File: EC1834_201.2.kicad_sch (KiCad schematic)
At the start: 69 parts, among them X4 Lautsprecher, X7 DB9_Female

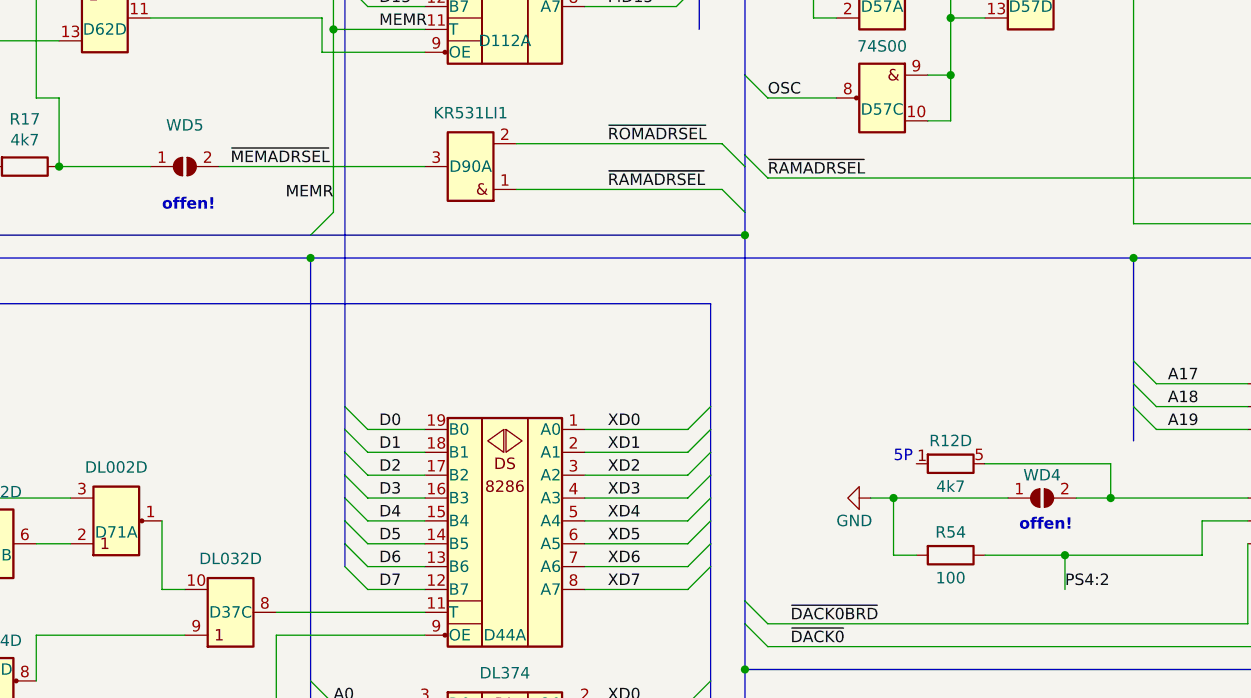
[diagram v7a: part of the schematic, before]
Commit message: Changed WD1-5 connections - open > bridged
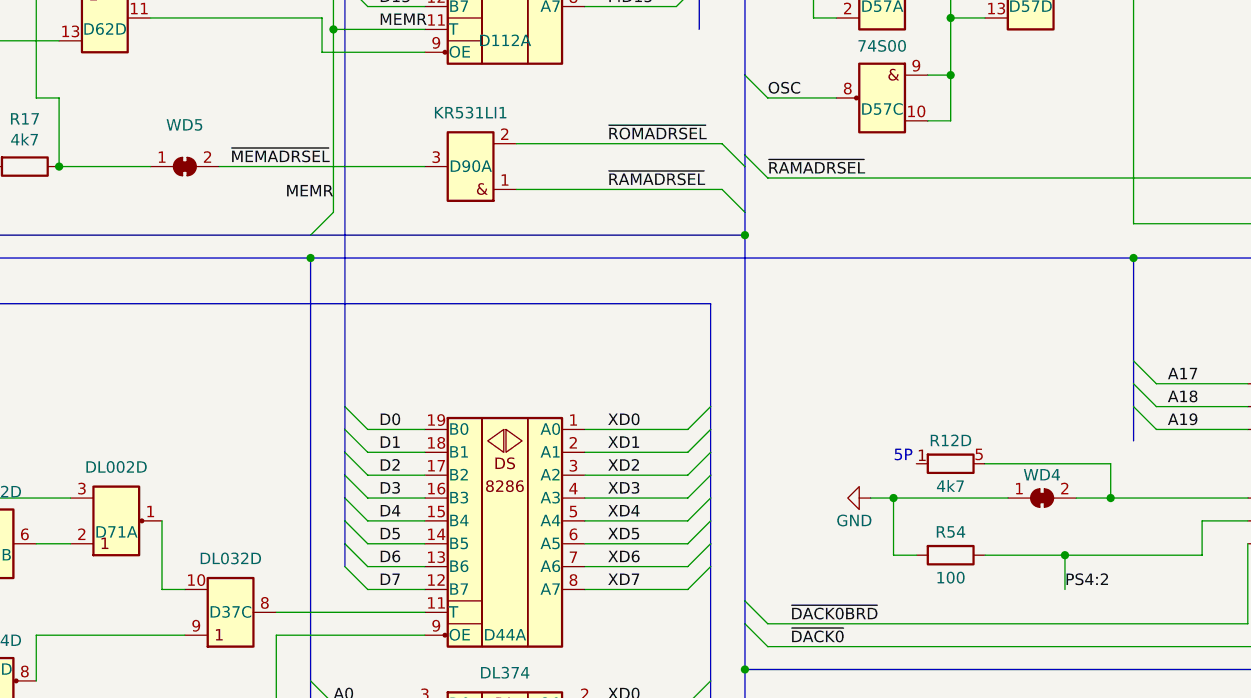
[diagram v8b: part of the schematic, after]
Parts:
- WD4, WD5: symbol Jumper:SolderJumper_2_Open -> Jumper:SolderJumper_2_Bridged
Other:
- note removed: "offen!"
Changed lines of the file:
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@@
     (effects (font (size 1.27 1.27)) (justify left bottom))
   )
-  (text "offen!" (at 118.11 184.15 0)
-    (effects (font (size 1.27 1.27) (thickness 0.254) bold) (justify left bottom))
-  )
   (text "entfällt \nauf 1834M!" (at 326.39 210.82 0)
     (effects (font (size 1.27 1.27)) (justify left bottom))
@@
     (effects (font (size 1.27 1.27)) (justify left bottom))
   )
-  (text "offen!" (at 213.36 219.71 0)
-    (effects (font (size 1.27 1.27) (thickness 0.254) bold) (justify left bottom))
-  )
   (text "entfällt \nauf 1834M!" (at 346.71 146.05 0)
     (effects (font (size 1.27 1.27)) (justify left bottom))
@@
     (pin "1")
   )
-  (symbol (lib_id "Jumper:SolderJumper_2_Open") (at 215.9 215.9 0) (unit 1)
+  (symbol (lib_id "Jumper:SolderJumper_2_Bridged") (at 215.9 215.9 0) (unit 1)
     (in_bom yes) (on_board yes)
     (property "Reference" "WD4" (id 0) (at 215.9 213.36 0))
@@
     (pin "1")
   )
-  (symbol (lib_id "Jumper:SolderJumper_2_Open") (at 120.65 179.07 0) (unit 1)
+  (symbol (lib_id "Jumper:SolderJumper_2_Bridged") (at 120.65 179.07 0) (unit 1)
     (in_bom yes) (on_board yes) (fields_autoplaced)
     (property "Reference" "WD5" (id 0) (at 120.65 174.4812 0))
